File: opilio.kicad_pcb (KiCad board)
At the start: 4 copper layers, 75 x 46 mm, 101 parts, among them J1 SATA_Power_Connector, J2 USB_C_Receptacle_USB2.0, J3 Conn_01x04_Male, J6 Conn_01x06_Male, Q1 CJ3134KW, Q2 NCE30P30K, SW1 Reset, SW2 Boot, U1 EUP3458, U2 STM32F103C8T6, U3 USBLC6-2SC6, Y1 TAXM8M4RFDCET2T, Y2 YST310S 32.768KHz

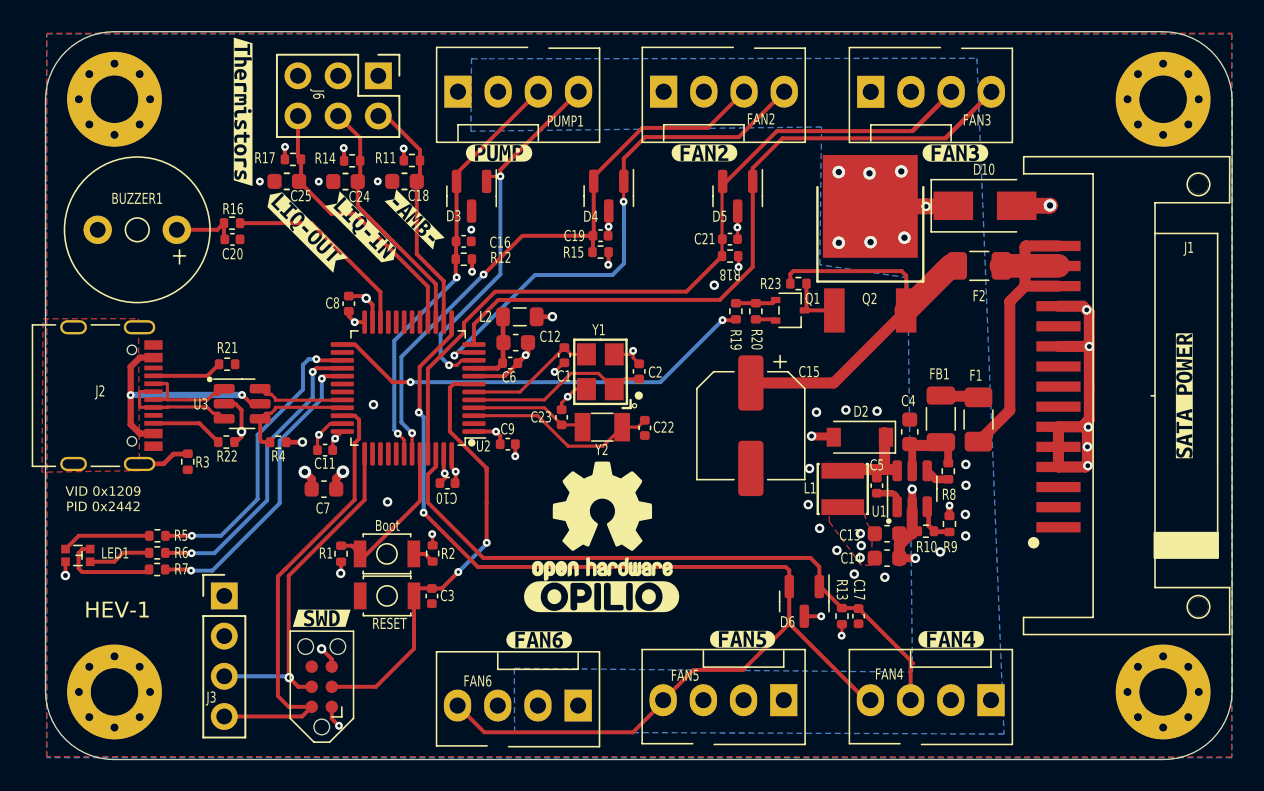
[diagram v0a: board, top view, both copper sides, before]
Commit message: double mosfets
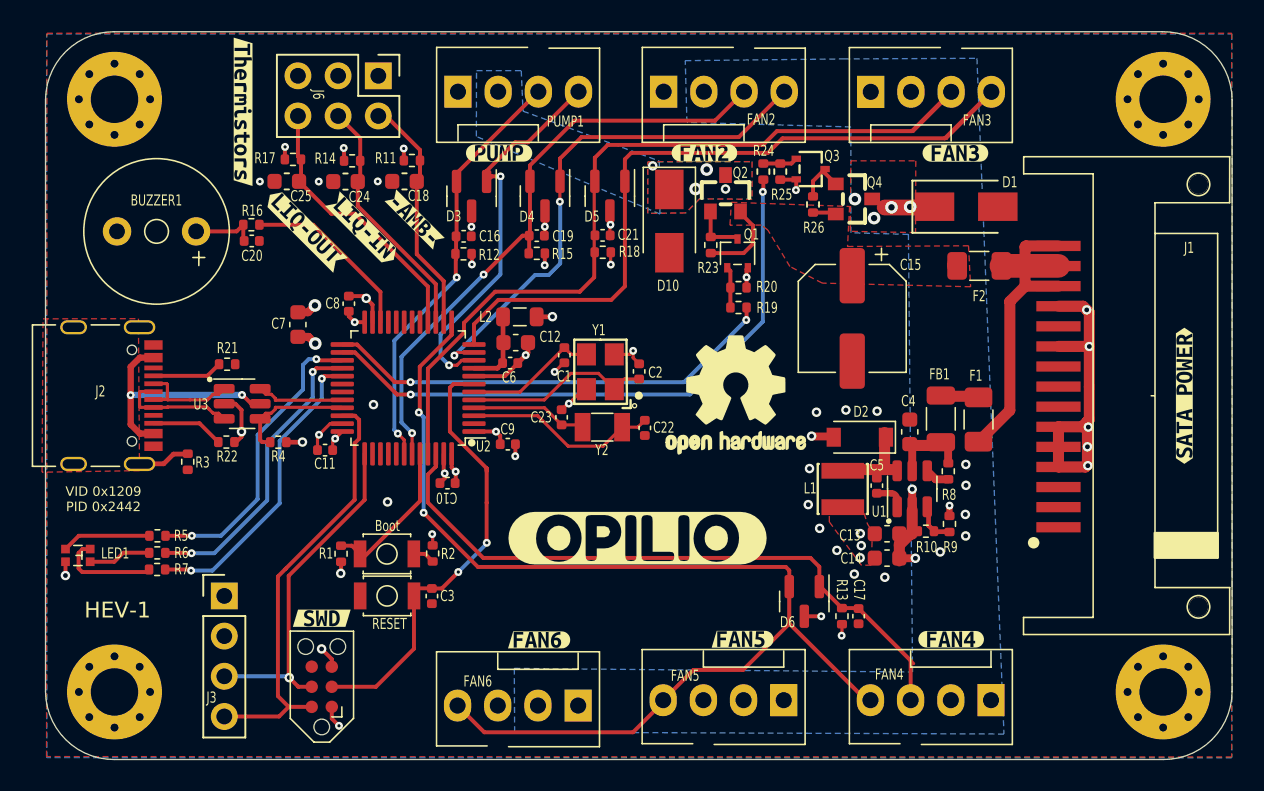
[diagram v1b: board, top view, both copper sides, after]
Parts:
- removed kibuzzard-63630189: G***, kibuzzard-63630189
- removed kibuzzard-6363019A: G***, kibuzzard-6363019A
- removed kibuzzard-63630213: G***, kibuzzard-63630213
- removed kibuzzard-636304F8: G***, kibuzzard-636304F8
- added D1: B230A, Diode_SMD:D_SMA, F.Cu at (163.3, 108.1)
- added Q3: CJ3134KW, easyeda2kicad:SC-70-3_L2.1-W1.3-P1.30-LS2.1-BR, F.Cu at (153.4, 105.7)
- added Q4: AO3401A, easyeda2kicad:SOT-23_L2.9-W1.3-P1.90-LS2.4-BR, F.Cu at (156.2, 107.6)
- added R24: 0R, Resistor_SMD:R_0402_1005Metric, F.Cu at (150.4, 105.9)
- added R25: 10K, Resistor_SMD:R_0402_1005Metric, F.Cu at (151.5, 105.9)
- added R26: 10K, Resistor_SMD:R_0402_1005Metric, F.Cu at (153.6, 107.9)
- added kibuzzard-63645B5C: G***, kibuzzard-63645B5C, F.Cu at (142.5, 129.0)
- added kibuzzard-6364685F: G***, kibuzzard-6364685F, F.Cu at (149.1, 135.4)
- added kibuzzard-63646865: G***, kibuzzard-63646865, F.Cu at (136.3, 135.5)
- added kibuzzard-636468A0: G***, kibuzzard-636468A0, F.Cu at (177.1, 120.0)
- Q2: value NCE30P30K -> AO3401A; footprint easyeda2kicad:TO-252-2_L6.6-W6.1-P4.57-LS9.9-TL-CW -> easyeda2kicad:SOT-23_L2.9-W1.3-P1.90-LS2.4-BR
- moved D10 20.0 mm to (144.5, 109.0), turned to -90 degrees
- moved LOGO1 11.6 mm to (148.7, 120.0)
- moved C7 10.5 mm to (121.0, 115.5), turned to 90 degrees
- moved Q2 10.0 mm to (148.1, 107.2), turned to -90 degrees
- moved C15 9.33 mm to (156.1, 115.1)
- moved D5 8.08 mm to (140.8, 107.4)
- moved C21 8.05 mm to (140.3, 109.9)
- moved R18 8.05 mm to (140.3, 111.0)
- moved R23 6.05 mm to (147.1, 110.5), turned to 90 degrees
- moved Q1 4.90 mm to (148.8, 111.0), turned to -90 degrees
- moved R15 4.03 mm to (136.1, 111.0)
- moved C19 4.03 mm to (136.1, 109.9)
- moved D4 4.03 mm to (136.7, 107.4)
- moved R20 1.86 mm to (148.9, 113.2), turned to 180 degrees
- moved C20 1.22 mm to (118.1, 110.2)
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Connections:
- net FET_GATE renamed PUMP_EN
- D10 pad 1: 12vC -> 12vP
- PUMP1 pad 2: 12vC -> 12vP
- Q2 pad 2: 12vC -> +12VF(F)
- Q2 pad 3: +12VF(F) -> 12vP
- U2 pad 26: unconnected-(U2-Pad26) -> FAN_EN
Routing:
- net FAN_EN: track 0.00 -> 38.6 mm, vias 0 -> 2
- net +12VF(F): track 26.5 -> 6.58 mm
- net PWM_OUT3: track 66.6 -> 59.3 mm
- net Net-(Q3-Pad3): track 0.00 -> 3.27 mm
- net Net-(Q3-Pad1): track 0.00 -> 2.20 mm
- net PWM_OUT1: track 23.7 -> 25.9 mm
- net 12vC: track 5.21 -> 3.34 mm, vias 7 -> 4
- net PWM_READ3: track 60.9 -> 62.6 mm
- net PUMP_EN: track 27.4 -> 28.9 mm
- net SWIO: track 29.0 -> 27.5 mm
- net BUZZER: track 12.6 -> 11.3 mm
- net GND: track 62.8 -> 61.9 mm
- net PWM_READ2: track 41.3 -> 42.0 mm
- net 12vP: vias 0 -> 4
- added copper zone on F.Cu, net +12VF(F)
- added copper zone on F.Cu, net 12vC
- added copper zone on B.Cu, net 12vP
- added copper zone on F.Cu, net 12vP

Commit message: move bottom esd diode
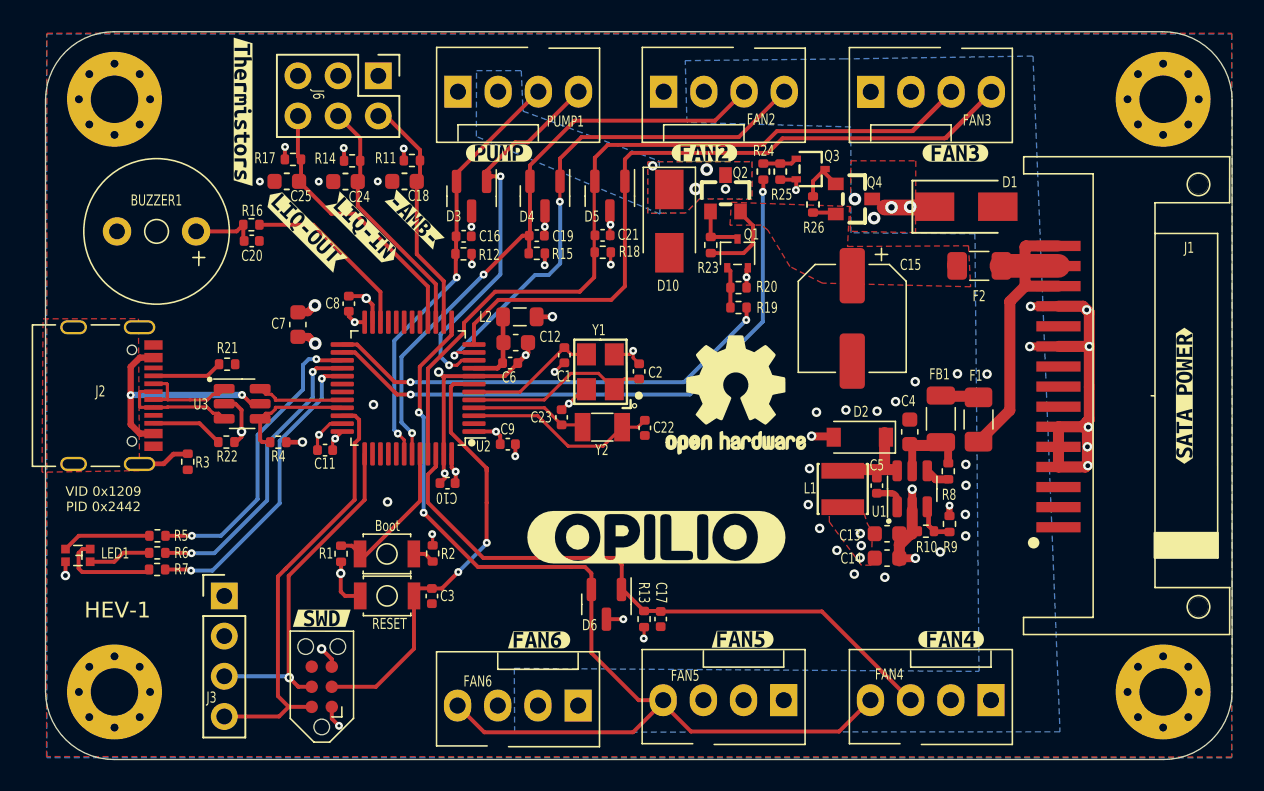
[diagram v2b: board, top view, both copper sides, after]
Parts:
- moved C17 12.5 mm to (144.0, 134.1)
- moved D6 12.5 mm to (140.5, 133.2)
- moved R13 12.5 mm to (142.9, 134.1)
- moved kibuzzard-63645B5C 1.19 mm to (143.7, 129.0)
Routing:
- net PWM_OUT4: track 81.5 -> 67.7 mm
- net GND: track 61.9 -> 75.6 mm, vias 46 -> 53
- net PWM_READ4: track 46.0 -> 39.8 mm

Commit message: match swd wires with bluepill
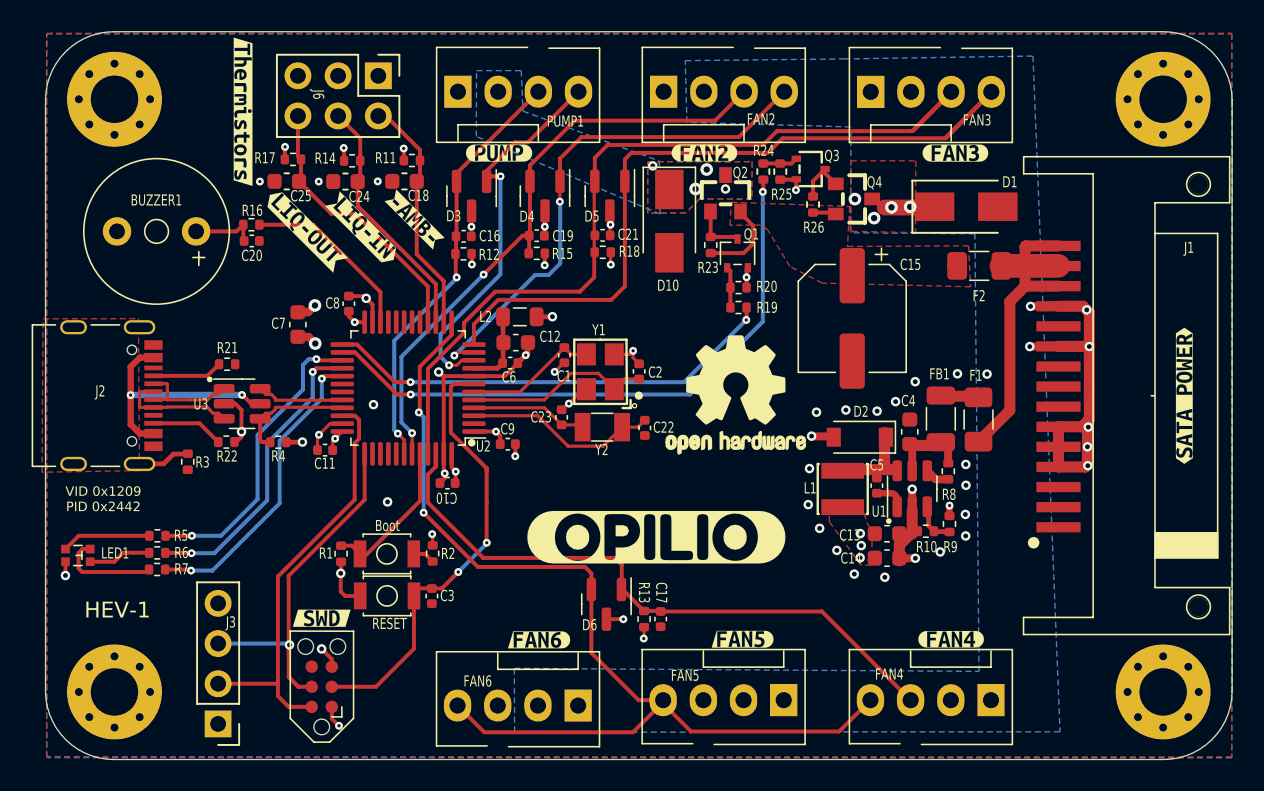
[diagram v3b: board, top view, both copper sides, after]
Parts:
- moved J3 8.10 mm to (116.0, 140.8), turned to 180 degrees
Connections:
- J3 pad 2: GND -> SWIO
- J3 pad 4: SWIO -> GND
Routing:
- net PWM_OUT4: track 67.7 -> 65.2 mm
- net SWIO: track 27.5 -> 27.0 mm

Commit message: before split schema
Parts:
- removed R2: 1K5, Resistor_SMD:R_0402_1005Metric
- removed kibuzzard-63630099: G***, kibuzzard-63630099
- removed kibuzzard-63645B5C: G***, kibuzzard-63645B5C
- added C26: 100nF, Capacitor_SMD:C_0402_1005Metric, F.Cu at (124.2, 128.4)
- added kibuzzard-6368E566: G***, kibuzzard-6368E566, F.Cu at (114.2, 133.4)
- added kibuzzard-6368E571: G***, kibuzzard-6368E571, F.Cu at (114.2, 135.8)
- added kibuzzard-6368E578: G***, kibuzzard-6368E578, F.Cu at (114.2, 138.3)
- added kibuzzard-6368E57E: G***, kibuzzard-6368E57E, F.Cu at (114.4, 140.7)
- added kibuzzard-6368E60E: G***, kibuzzard-6368E60E, F.Cu at (126.8, 128.2)
- added kibuzzard-6368E619: G***, kibuzzard-6368E619, F.Cu at (126.7, 134.5)
- added kibuzzard-6368E624: G***, kibuzzard-6368E624, F.Cu at (122.5, 134.1)
- added kibuzzard-6368E8DC: G***, kibuzzard-6368E8DC, F.Cu at (143.7, 128.4)
- R1: value 100K -> 10K
- R3: value 100K -> 75K
- moved J3 0.99 mm to (117.0, 140.6)
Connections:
- SW2 pad 2: Net-(R2-Pad2) -> +3.3V
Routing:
- net GND: track 75.6 -> 85.1 mm, vias 53 -> 56
- net BOOT0: track 9.84 -> 11.6 mm
- net Net-(R2-Pad2): track 1.39 -> 0.00 mm
- net SWCLK: track 22.4 -> 21.2 mm
- net SWIO: track 27.0 -> 26.0 mm
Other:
- board text added: "REV-7"
- board text removed: "HEV-1"
